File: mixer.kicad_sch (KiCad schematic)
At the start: 14 parts, among them Q4 MMBT3904

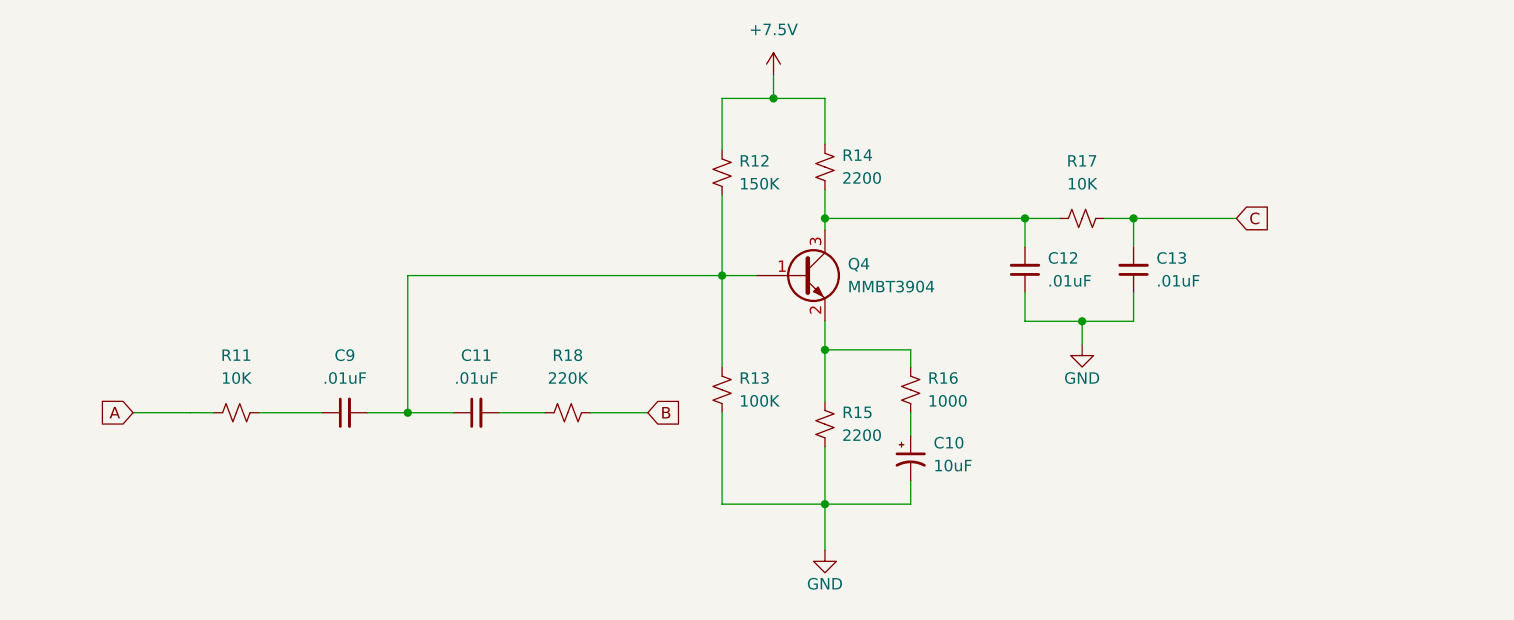
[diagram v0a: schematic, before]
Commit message: Components mostly placed
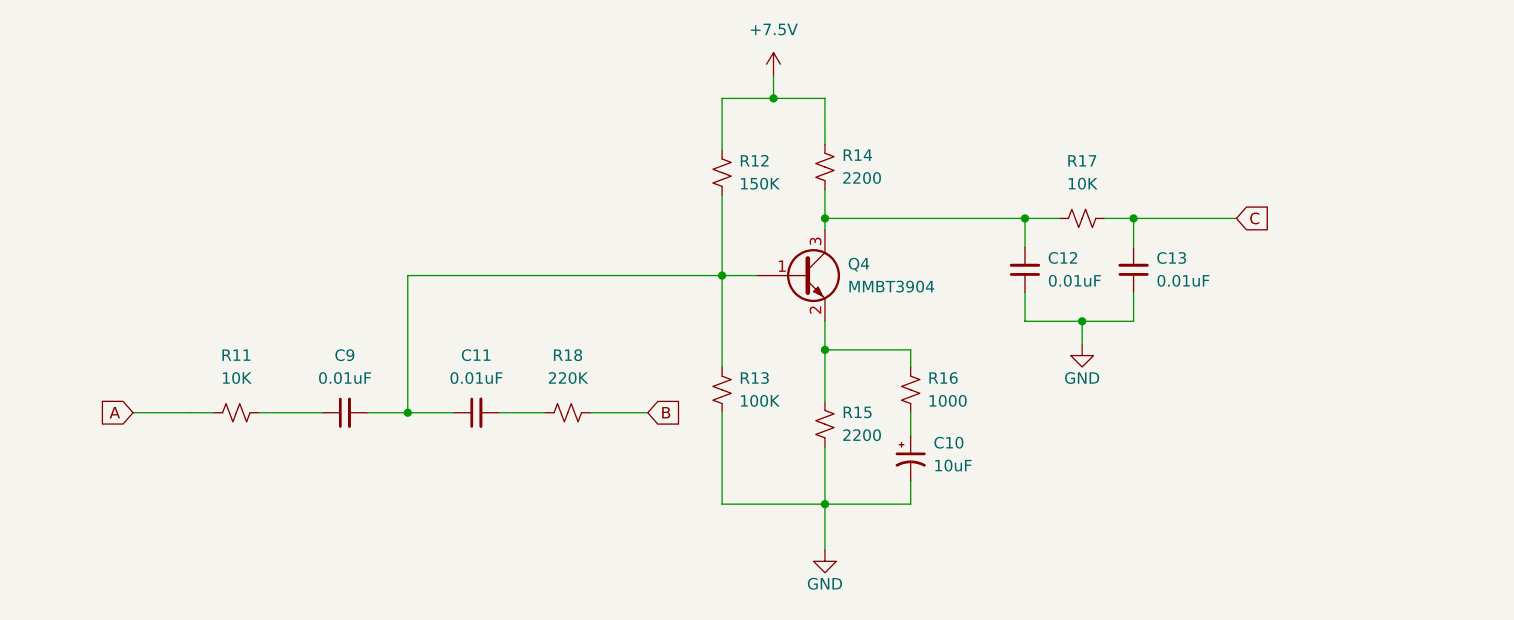
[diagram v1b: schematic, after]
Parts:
- C11, C12, C13, C9: value .01uF -> 0.01uF
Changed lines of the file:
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@@
     (in_bom yes) (on_board yes) (fields_autoplaced)
     (property "Reference" "C11" (id 0) (at 122.5613 106.045 90))
-    (property "Value" ".01uF" (id 1) (at 122.5613 108.585 90))
+    (property "Value" "0.01uF" (id 1) (at 122.5613 108.585 90))
     (property "Footprint" "Capacitor_SMD:C_0603_1608Metric" (id 2) (at 122.555 112.395 0)
       (effects (font (size 1.27 1.27)) hide)
@@
       (effects (font (size 1.27 1.27)) (justify right))
     )
-    (property "Value" ".01uF" (id 1) (at 198.12 97.7835 0)
+    (property "Value" "0.01uF" (id 1) (at 198.12 97.7835 0)
       (effects (font (size 1.27 1.27)) (justify right))
     )
@@
     (in_bom yes) (on_board yes) (fields_autoplaced)
     (property "Reference" "C9" (id 0) (at 107.9563 106.045 90))
-    (property "Value" ".01uF" (id 1) (at 107.9563 108.585 90))
+    (property "Value" "0.01uF" (id 1) (at 107.9563 108.585 90))
     (property "Footprint" "Capacitor_SMD:C_0603_1608Metric" (id 2) (at 107.95 112.395 0)
       (effects (font (size 1.27 1.27)) hide)
@@
       (effects (font (size 1.27 1.27)) (justify right))
     )
-    (property "Value" ".01uF" (id 1) (at 186.055 97.7835 0)
-      (effects (font (size 1.27 1.27)) (justify right))
-    )
+    (property "Value" "0.01uF" (id 1) (at 186.055 97.7835 0)
+      (effects (font (size 1.27 1.27)) (justify right))
+    )

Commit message: Better component placements
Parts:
- added JP1: A, Jumper:SolderJumper-2_P1.3mm_Open_RoundedPad1.0x1.5mm, symbol Jumper:SolderJumper_2_Open
- added JP2: B, Jumper:SolderJumper-2_P1.3mm_Open_RoundedPad1.0x1.5mm, symbol Jumper:SolderJumper_2_Open
- added JP3: C, Jumper:SolderJumper-2_P1.3mm_Open_RoundedPad1.0x1.5mm, symbol Jumper:SolderJumper_2_Open
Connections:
- net A: now also JP1.1 (A); no longer R11.1
- net B: now also JP2.2 (B); no longer R18.2
- net C: now also JP3.2 (B); no longer C13.2, R17.2
- new net: JP2.1 (A), R18.2
- new net: C13.2, JP3.1 (A), R17.2
- new net: JP1.2 (B), R11.1
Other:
- moved on the sheet: C10, C11, C12, C13, C9, Q4, R11, R12, R13, R14, R15, R16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
